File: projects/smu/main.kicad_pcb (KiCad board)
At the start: 4 copper layers, 100 x 100 mm, 69 parts, among them P101 CONN_01X15, P102 CONN_01X28, U301 LM741, U302 DG444, U303 LM741, U304 LM741, U305 LM311N, U401 DAC8734, U402 LM324, U404 LM324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

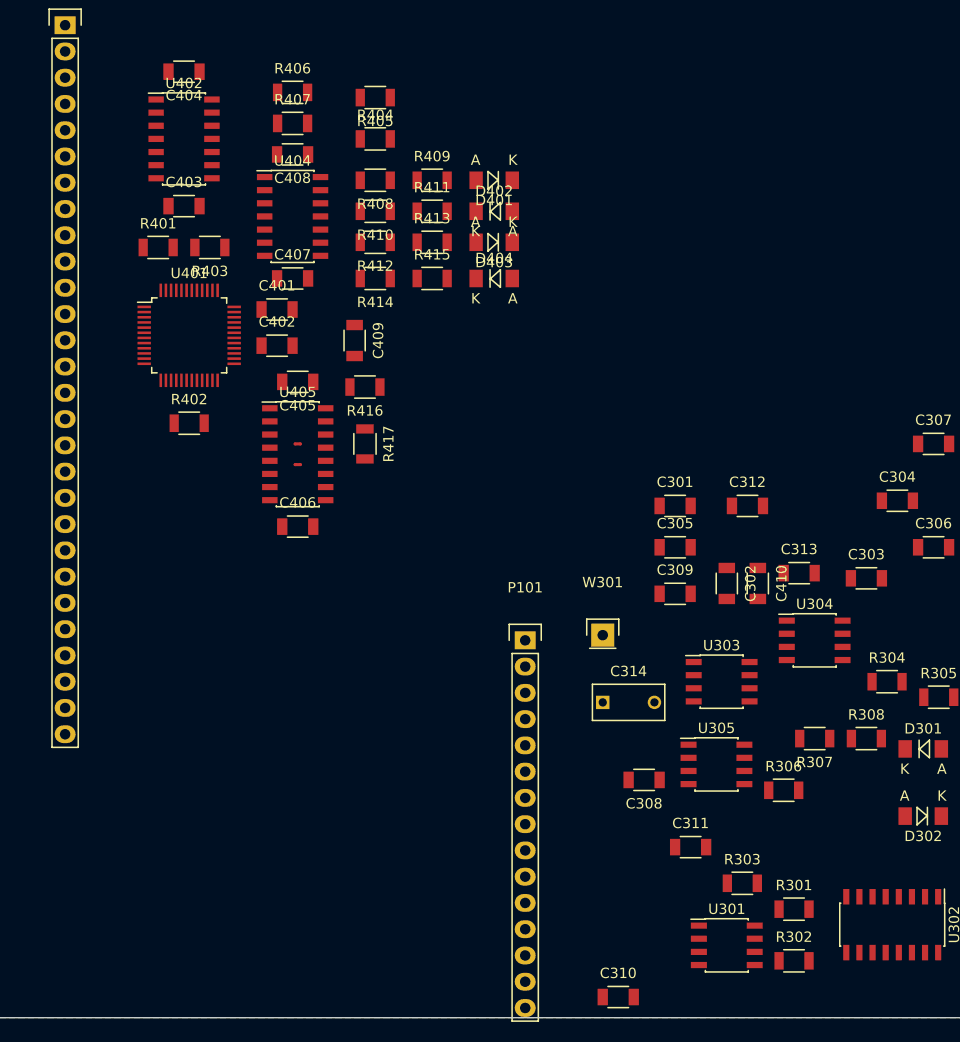
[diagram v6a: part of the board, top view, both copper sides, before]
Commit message: add lt1021, remove net-tie
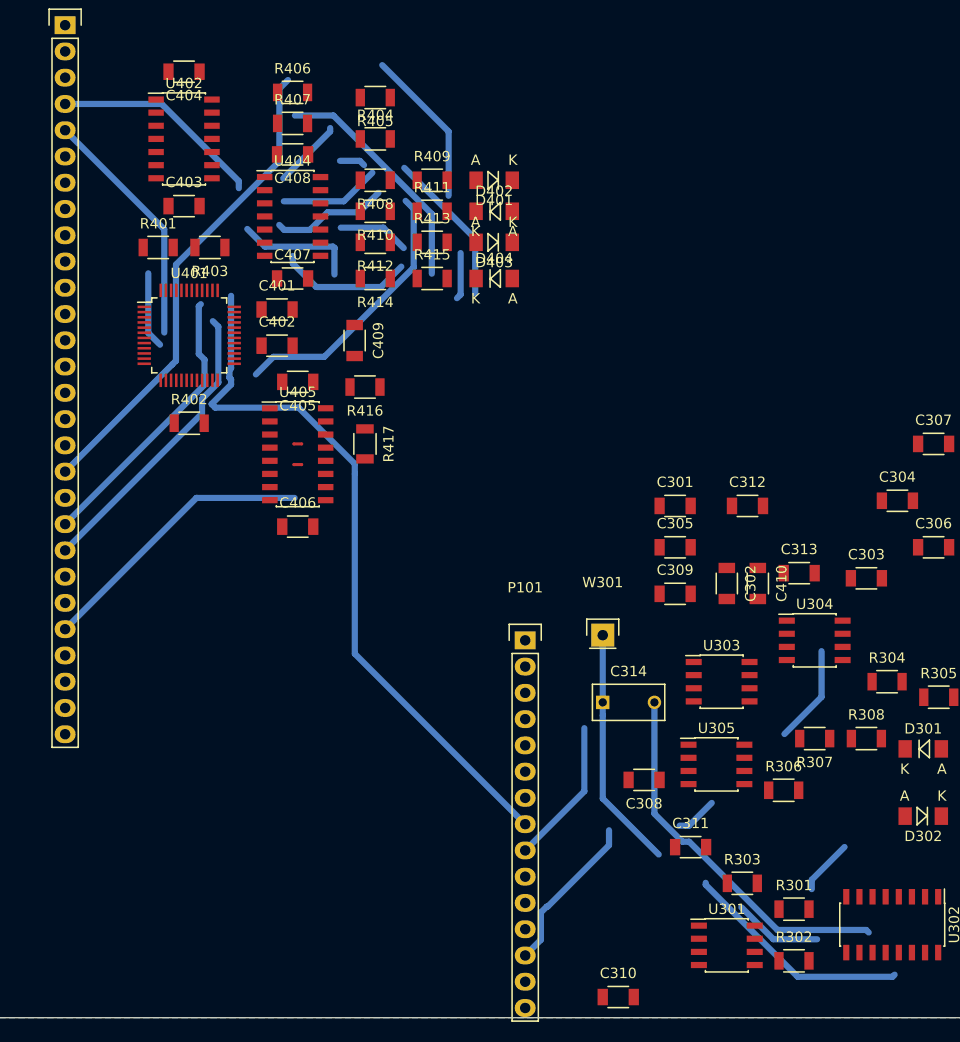
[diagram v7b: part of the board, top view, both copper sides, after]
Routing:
- net (no net): track 0.00 -> 205.3 mm
- net 3.3V: track 0.00 -> 69.3 mm
- net V-SET: track 0.00 -> 46.8 mm
- net Net-(C311-Pad2): track 0.00 -> 36.3 mm
- net V-OUT-4: track 0.00 -> 28.5 mm
- net REF_IN2: track 0.00 -> 27.5 mm
- net V-OUT-3: track 0.00 -> 27.2 mm
- net REF: track 0.00 -> 23.5 mm
- net Net-(C311-Pad1): track 0.00 -> 23.5 mm
- net OUT: track 0.00 -> 20.6 mm
- net TRIGGER: track 0.00 -> 15.5 mm
- net REF_PLUS_CTL: track 0.00 -> 14.2 mm
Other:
- net class Default: clearance 0.3 -> 0.2
- net class dac: trace_width 0.2 -> 0.29; via_dia 0.6 -> 0.5; via_drill 0.4 -> 0.3
- rule trace_clearance: 0.3 -> 0.2
